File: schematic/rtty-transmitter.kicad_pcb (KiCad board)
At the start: 2 copper layers, 120 x 60 mm, 75 parts, among them J1 USB Type B Connector, J2 USBasp header, J3 2x5 Pin Header Connector Fema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, J4 Conn_01x02_Pin, J5 Conn_01x02_Pin, J6 Conn_01x02_Pin, J7 SMA Vertical Female, Q1 PN2222A, Q2 PN2222A, U1 MCP2221AxP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

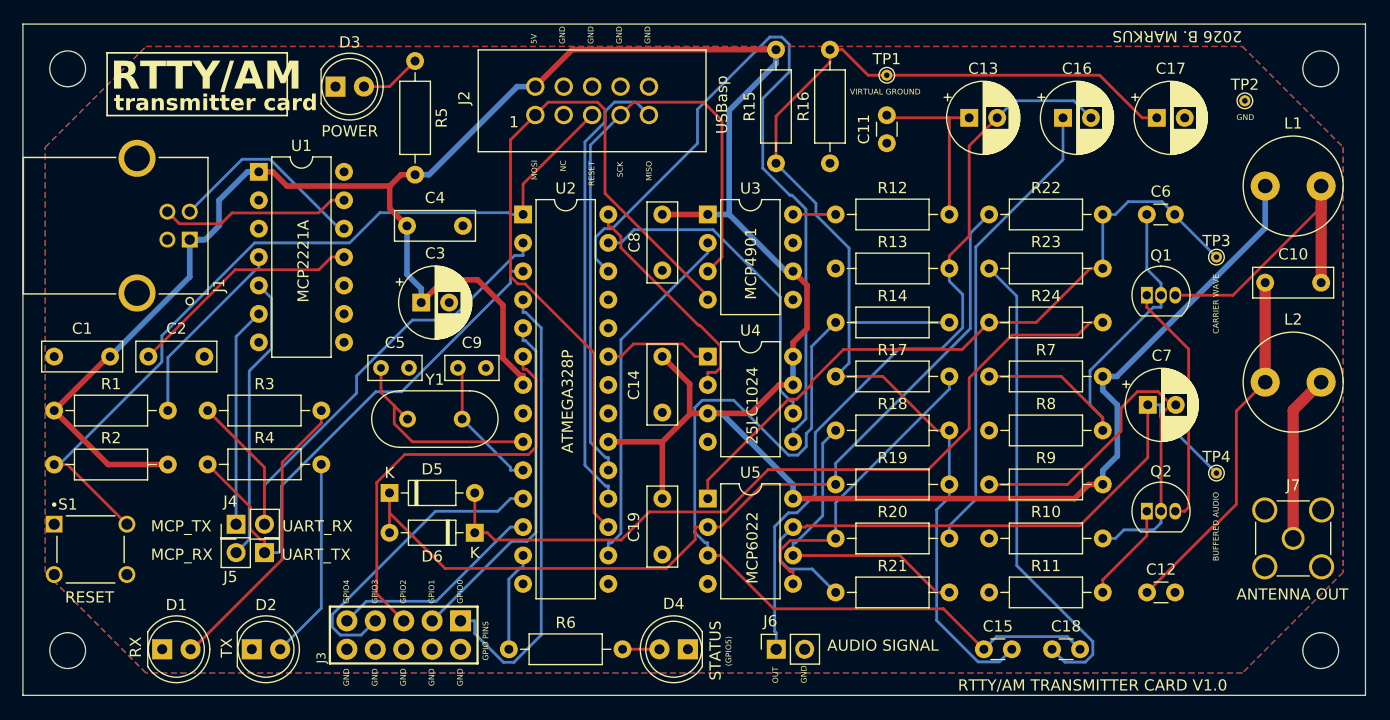
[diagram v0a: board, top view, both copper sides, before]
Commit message: PCB updated: electrolytic capacitor footprints updated
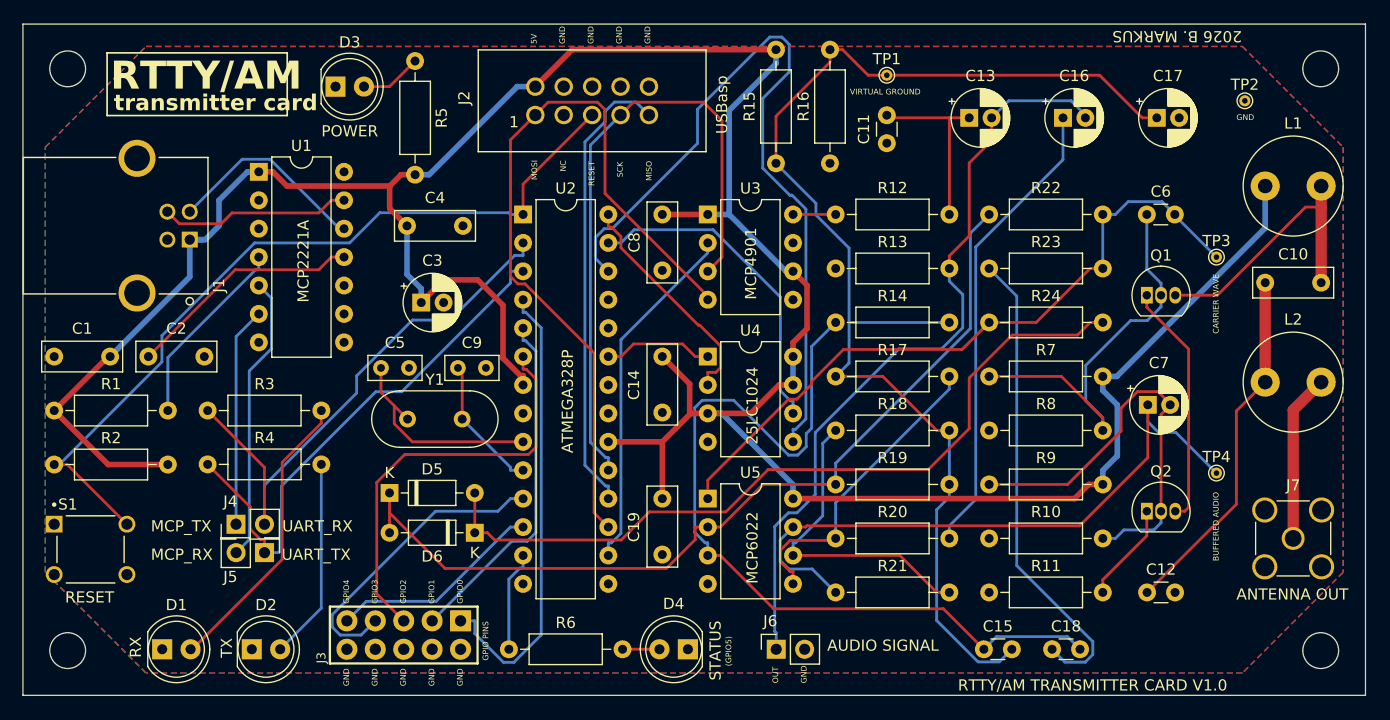
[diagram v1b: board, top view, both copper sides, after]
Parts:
- C13, C16, C17, C3, C7: footprint Capacitor_THT:CP_Radial_D6.3mm_P2.50mm -> Capacitor_THT:CP_Radial_D5.0mm_P2.00mm
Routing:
- net Net-(Q1-B): track 36.2 -> 36.9 mm

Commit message: PCB updated: resistor footprints updated
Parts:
- R9: footprint StockLib:R_10k_Axial_DIN0207 -> StockLib:R_470_Axial_DIN0207
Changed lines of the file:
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@@
     )
   )
-  (footprint "StockLib:R_10k_Axial_DIN0207" (layer "F.Cu")
+  (footprint "StockLib:R_470_Axial_DIN0207" (layer "F.Cu")
     (at 86.36 41.148)
     (descr "Resistor, Axial_DIN0207 series, Axial, Horizontal, pin pitch=10.16mm, 0.25W = 1/4W, length*diameter=6.3*2.5mm^2, http://cdn-reichelt.de/documents/datenblatt/B400/1_4W%23YAG.pdf")
@@
     (pad "2" thru_hole oval (at 10.16 0) (size 1.6 1.6) (drill 0.8) (layers "*.Cu" "*.Mask")
       (net 5 "+5V") (pintype "passive"))
-    (model "C:/Users/bazsi/Documents/KiCad/7.0/3dmodels/Resistors/Res-10.16-6.3x2.3-10k.step"
+    (model "C:/Users/bazsi/Documents/KiCad/7.0/3dmodels/Resistors/Res-10.16-6.3x2.3-470.step"
       (offset (xyz 5 0 0))
       (scale (xyz 1 1 1))
